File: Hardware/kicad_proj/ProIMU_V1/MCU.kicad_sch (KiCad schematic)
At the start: 10 parts

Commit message: Update: Schematic
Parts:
- added U?: AIR602, footprints:AIR602, symbol air602:AIR602
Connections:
- net +3V3: now also U?.4 (VCC)
- net GND: now also U?.1 (GND), U?.3 (GND)
- net WIFI_RES: now also U?.12 (RES)
- net WIFI_UART_RX: now also U?.5 (TX0)
- net WIFI_UART_TX: now also U?.6 (RX0)
- new net ANT: U?.2 (ANT)
- no-connect marks 13 -> 18
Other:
- note added: "WiFi:"
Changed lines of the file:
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@@
   (junction (at 101.6 137.16) (diameter 0) (color 0 0 0 0)
   )
+  (no_connect (at 254.635 104.14))
   (no_connect (at 111.125 105.41))
   (no_connect (at 169.545 36.83))
@@
   (no_connect (at 169.545 39.37))
   (no_connect (at 111.125 107.95))
+  (no_connect (at 254.635 111.76))
   (no_connect (at 111.125 110.49))
   (no_connect (at 111.125 36.83))
   (no_connect (at 111.125 77.47))
+  (no_connect (at 254.635 114.3))
   (no_connect (at 169.545 44.45))
   (no_connect (at 111.125 34.29))
+  (no_connect (at 254.635 106.68))
   (no_connect (at 169.545 46.99))
   (no_connect (at 111.125 46.99))
   (no_connect (at 111.125 52.07))
+  (no_connect (at 254.635 109.22))
   (wire (pts (xy 109.22 137.16) (xy 101.6 137.16))
     (stroke (width 0) (type default) (color 0 0 0 0))
@@
     (stroke (width 0) (type default) (color 0 0 0 0))
   )
+  (polyline (pts (xy 223.52 86.36) (xy 223.52 126.365))
+    (stroke (width 0) (type default) (color 0 0 0 0))
+  )
+  (polyline (pts (xy 223.52 126.365) (xy 269.875 126.365))
+    (stroke (width 0) (type default) (color 0 0 0 0))
+  )
+  (polyline (pts (xy 223.52 127) (xy 223.52 129.54))
+    (stroke (width 0) (type default) (color 0 0 0 0))
+  )
   (wire (pts (xy 163.195 36.83) (xy 169.545 36.83))
     (stroke (width 0) (type default) (color 0 0 0 0))
@@
     (stroke (width 0) (type default) (color 0 0 0 0))
   )
+  (wire (pts (xy 232.41 104.14) (xy 234.315 104.14))
+    (stroke (width 0) (type default) (color 0 0 0 0))
+  )
   (wire (pts (xy 163.83 152.4) (xy 161.29 152.4))
     (stroke (width 0) (type default) (color 0 0 0 0))
   )
+  (polyline (pts (xy 269.875 86.36) (xy 223.52 86.36))
+    (stroke (width 0) (type default) (color 0 0 0 0))
+  )
   (wire (pts (xy 100.965 97.79) (xy 111.125 97.79))
     (stroke (width 0) (type default) (color 0 0 0 0))
@@
     (stroke (width 0) (type default) (color 0 0 0 0))
   )
+  (wire (pts (xy 231.775 109.22) (xy 234.315 109.22))
+    (stroke (width 0) (type default) (color 0 0 0 0))
+  )
   (wire (pts (xy 132.08 129.54) (xy 140.335 129.54))
     (stroke (width 0) (type default) (color 0 0 0 0))
@@
     (stroke (width 0) (type default) (color 0 0 0 0))
   )
+  (polyline (pts (xy 269.875 129.54) (xy 269.875 126.365))
+    (stroke (width 0) (type default) (color 0 0 0 0))
+  )
+  (wire (pts (xy 234.315 114.3) (xy 234.315 120.015))
+    (stroke (width 0) (type default) (color 0 0 0 0))
+  )
   (wire (pts (xy 39.37 171.45) (xy 40.64 171.45))
     (stroke (width 0) (type default) (color 0 0 0 0))
@@
     (stroke (width 0) (type default) (color 0 0 0 0))
   )
+  (wire (pts (xy 234.315 93.345) (xy 234.315 99.06))
+    (stroke (width 0) (type default) (color 0 0 0 0))
+  )
   (wire (pts (xy 161.29 147.32) (xy 171.45 147.32))
     (stroke (width 0) (type default) (color 0 0 0 0))
@@
     (stroke (width 0) (type default) (color 0 0 0 0))
   )
+  (wire (pts (xy 254.635 101.6) (xy 256.54 101.6))
+    (stroke (width 0) (type default) (color 0 0 0 0))
+  )
   (wire (pts (xy 106.68 157.48) (xy 109.22 157.48))
     (stroke (width 0) (type default) (color 0 0 0 0))
   )
+  (polyline (pts (xy 223.52 129.54) (xy 269.875 129.54))
+    (stroke (width 0) (type default) (color 0 0 0 0))
+  )
   (wire (pts (xy 39.37 156.21) (xy 40.64 156.21))
     (stroke (width 0) (type default) (color 0 0 0 0))
@@
     (stroke (width 0) (type default) (color 0 0 0 0))
   )
+  (wire (pts (xy 254.635 99.06) (xy 256.54 99.06))
+    (stroke (width 0) (type default) (color 0 0 0 0))
+  )
   (wire (pts (xy 100.965 90.17) (xy 111.125 90.17))
     (stroke (width 0) (type default) (color 0 0 0 0))
@@
     (stroke (width 0) (type default) (color 0 0 0 0))
   )
+  (polyline (pts (xy 269.875 86.36) (xy 269.875 126.365))
+    (stroke (width 0) (type default) (color 0 0 0 0))
+  )
   (wire (pts (xy 102.235 49.53) (xy 111.125 49.53))
     (stroke (width 0) (type default) (color 0 0 0 0))
@@
     (stroke (width 0) (type default) (color 0 0 0 0))
   )
+  (text "WiFi:" (at 224.155 128.905 0)
+    (effects (font (size 1.27 1.27)) (justify left bottom))
+  )
   (label "SDCARD_D2" (at 39.37 163.83 180)
     (effects (font (size 1.27 1.27)) (justify right bottom))
@@
     (effects (font (size 1.27 1.27)) (justify right bottom))
   )
+  (label "ANT" (at 231.775 109.22 180)
+    (effects (font (size 1.27 1.27)) (justify right bottom))
+  )
+  (label "WIFI_RES" (at 232.41 104.14 180)
+    (effects (font (size 1.27 1.27)) (justify right bottom))
+  )
   (label "SDACRD_DET_SWT" (at 39.37 168.91 180)
     (effects (font (size 1.27 1.27)) (justify right bottom))
@@
   (label "SDCARD_CMD" (at 102.235 49.53 180)
     (effects (font (size 1.27 1.27)) (justify right bottom))
+  )
+  (label "WIFI_UART_TX" (at 256.54 101.6 0)
+    (effects (font (size 1.27 1.27)) (justify left bottom))
   )
   (label "CAN_TRX+" (at 100.965 100.33 180)
@@
   (label "SDCARD_D2" (at 102.235 57.15 180)
     (effects (font (size 1.27 1.27)) (justify right bottom))
+  )
+  (label "WIFI_UART_RX" (at 256.54 99.06 0)
+    (effects (font (size 1.27 1.27)) (justify left bottom))
   )
   (label "USB+" (at 102.235 64.77 180)
@@
     (pin "1")
   )
+  (symbol (lib_id "power:GND") (at 234.315 120.015 0) (unit 1)
+    (in_bom yes) (on_board yes) (fields_autoplaced)
+    (property "Reference" "#PWR?" (id 0) (at 234.315 126.365 0)
+      (effects (font (size 1.27 1.27)) hide)
+    )
+    (property "Value" "GND" (id 1) (at 234.315 125.095 0))
+    (property "Footprint" "" (id 2) (at 234.315 120.015 0)
+      (effects (font (size 1.27 1.27)) hide)
+    )
+    (property "Datasheet" "" (id 3) (at 234.315 120.015 0)
+      (effects (font (size 1.27 1.27)) hide)
+    )
+    (pin "1")
+  )
   (symbol (lib_id "power:+3V3") (at 171.45 133.35 0) (unit 1)
     (in_bom yes) (on_board yes) (fields_autoplaced)
@@
     (pin "2")
   )
+  (symbol (lib_id "power:+3V3") (at 234.315 93.345 0) (unit 1)
+    (in_bom yes) (on_board yes) (fields_autoplaced)
+    (property "Reference" "#PWR?" (id 0) (at 234.315 97.155 0)
+      (effects (font (size 1.27 1.27)) hide)
+    )
+    (property "Value" "+3V3" (id 1) (at 234.315 87.63 0))
+    (property "Footprint" "" (id 2) (at 234.315 93.345 0)
+      (effects (font (size 1.27 1.27)) hide)
+    )
+    (property "Datasheet" "" (id 3) (at 234.315 93.345 0)
+      (effects (font (size 1.27 1.27)) hide)
+    )
+    (pin "1")
+  )
+  (symbol (lib_id "air602:AIR602") (at 244.475 106.68 0) (unit 1)
+    (in_bom yes) (on_board yes) (fields_autoplaced)
+    (property "Reference" "U?" (id 0) (at 244.475 90.805 0))
+    (property "Value" "AIR602" (id 1) (at 244.475 93.345 0))
+    (property "Footprint" "footprints:AIR602" (id 2) (at 244.475 106.68 0)
+      (effects (font (size 1.27 1.27)) hide)
+    )
+    (property "Datasheet" "" (id 3) (at 244.475 106.68 0)
+      (effects (font (size 1.27 1.27)) hide)
+    )
+    (pin "1")
+    (pin "10")
+    (pin "11")
+    (pin "12")
+    (pin "2")
+    (pin "3")
+    (pin "4")
+    (pin "5")
+    (pin "6")
+    (pin "7")
+    (pin "8")
+    (pin "9")
+  )
   (symbol (lib_id "Device:C_Small") (at 114.3 125.095 0) (unit 1)

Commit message: Update: Schematic
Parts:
- removed U?: AIR602, footprints:AIR602, symbol air602:AIR602
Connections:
- no-connect marks 18 -> 13
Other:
- note removed: "WiFi:"

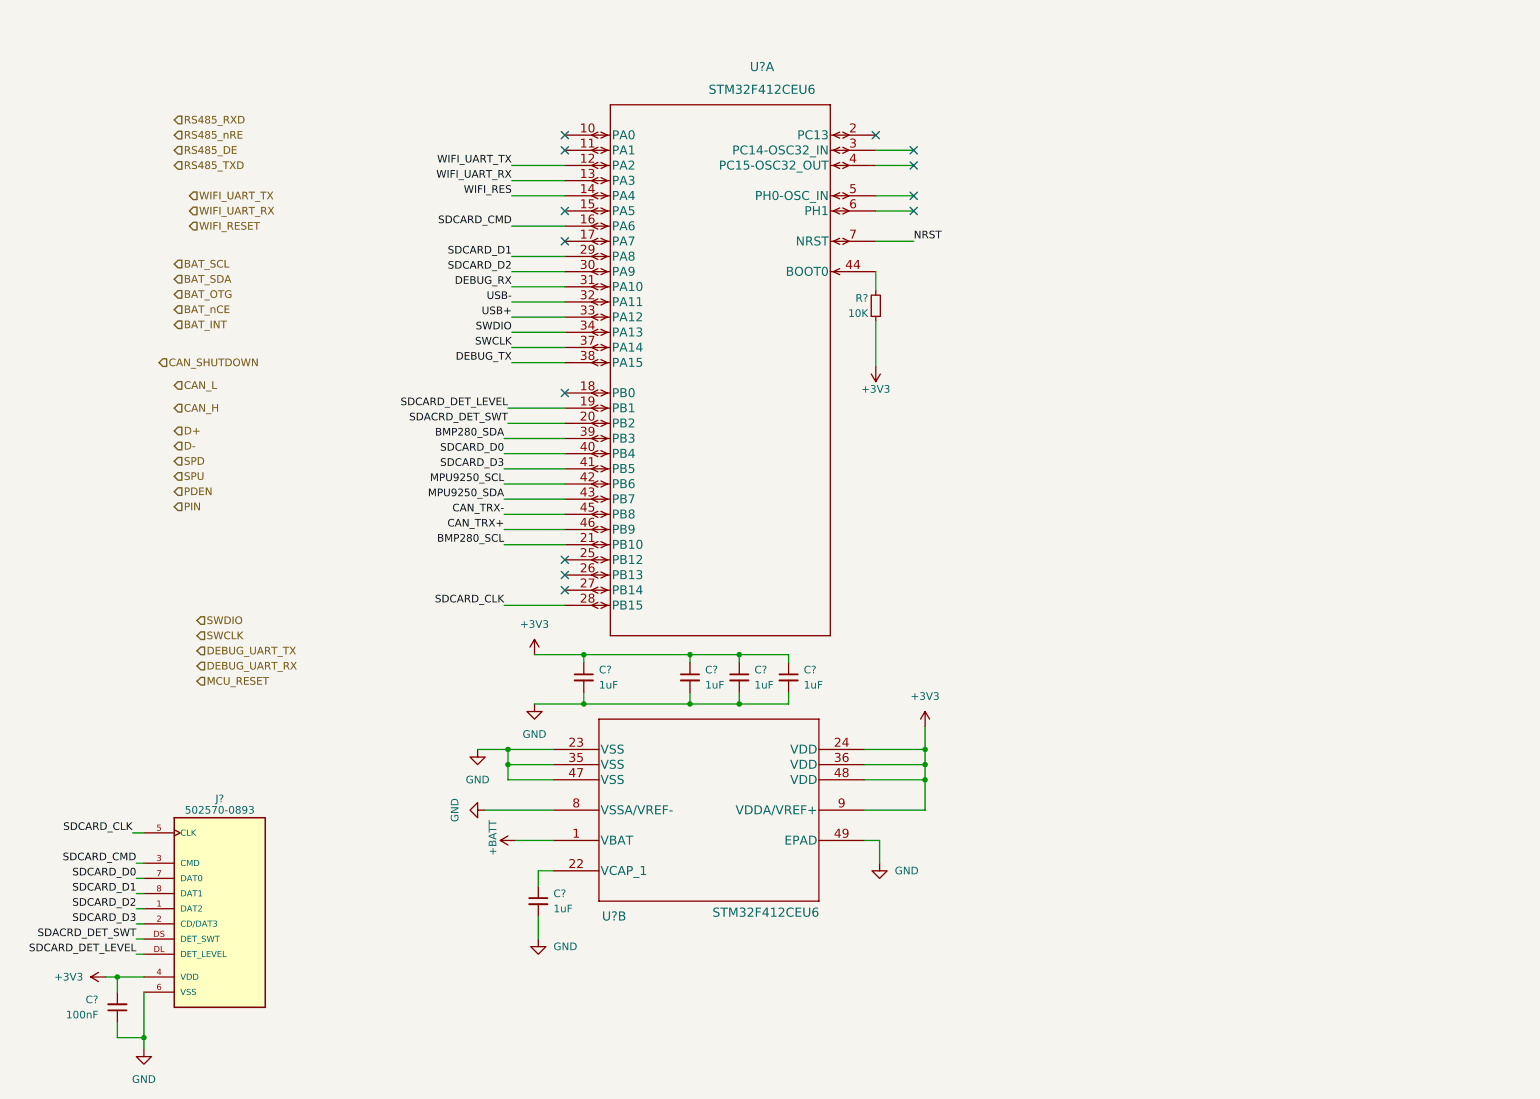
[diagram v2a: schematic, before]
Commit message: Schematic Updated. Removed unecessary schematic pages
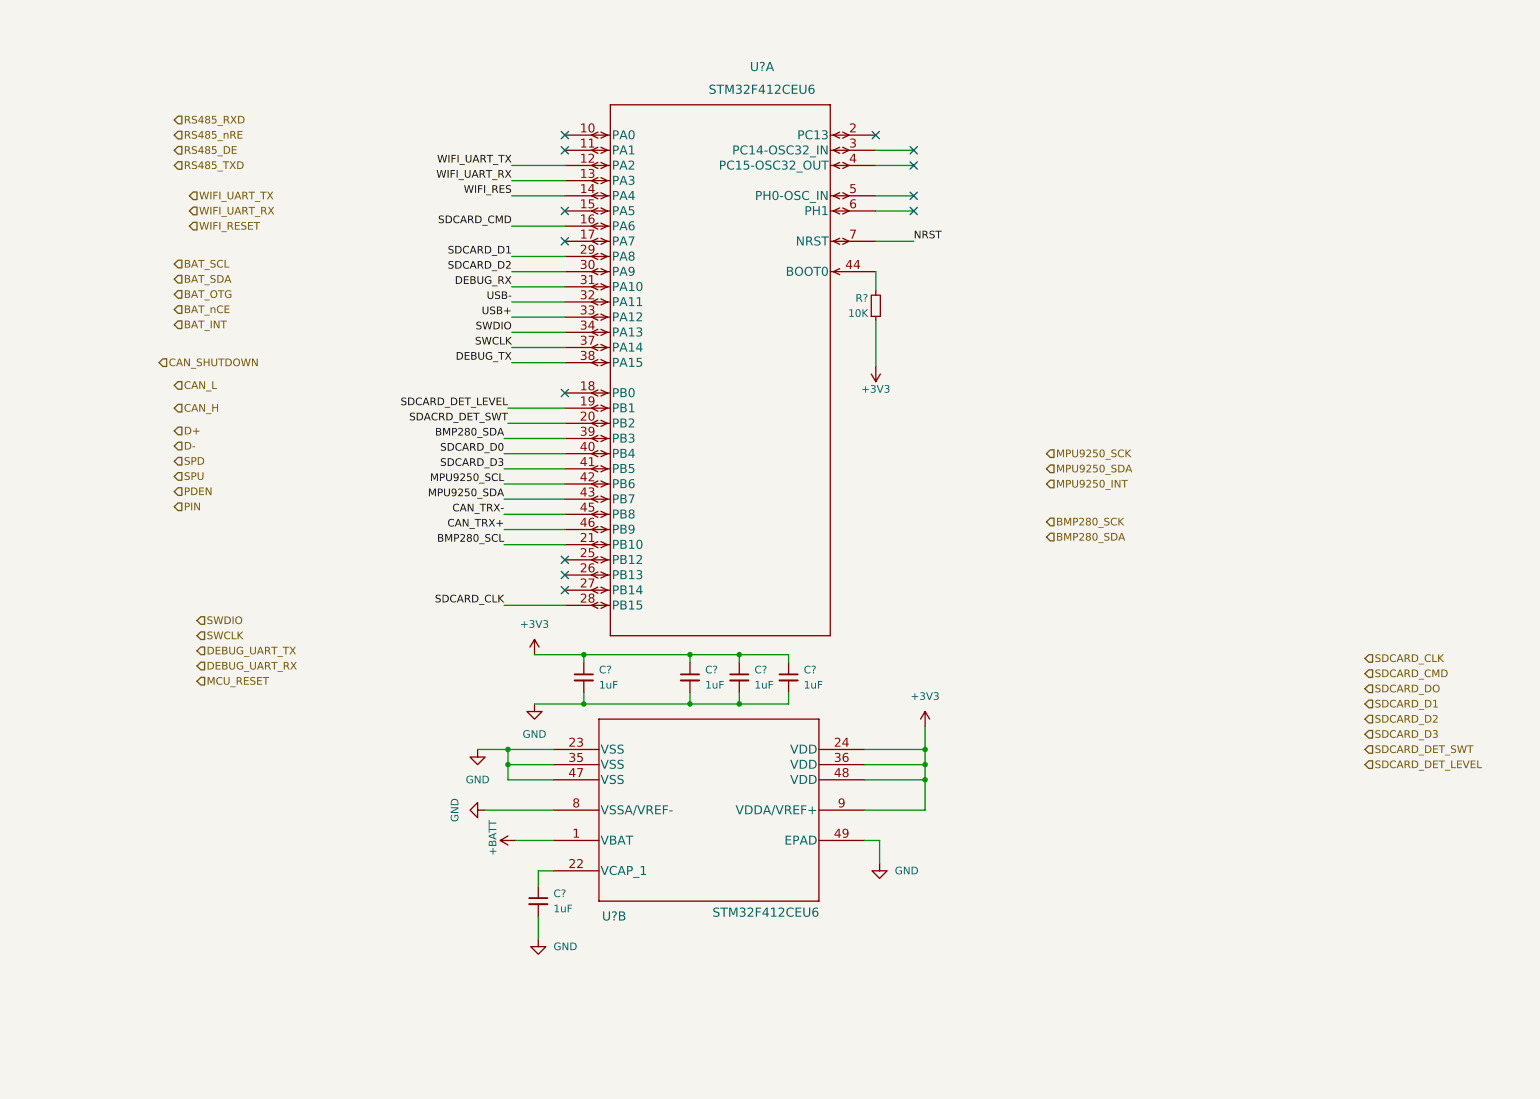
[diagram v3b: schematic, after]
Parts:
- removed C?: 100nF, Capacitor_SMD:C_0402_1005Metric_Pad0.74x0.62mm_HandSolder, symbol Device:C_Small
- removed J?: 502570-0893, footprints:MOLEX_502570-0893, symbol 502570-0893:502570-0893
